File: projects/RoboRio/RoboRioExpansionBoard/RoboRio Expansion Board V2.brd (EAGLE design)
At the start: 56.6 x 77.5 mm, 133 parts, among them J1 RRINTERFACE-FEMALE, J10 SPI_MISO, J11 SPI_MOSI, J12 I2C_SCL, J13 I2C_SDA, J14 UART_TX, J15 UART_RX, J16 LCD, J17 ADC1, J18 ADC2, J19 ADC3, J2 MICROSD-HINGED, J20 ADC4, J21 ADC5, J22 ADC6, J23 ADC7, J25 PWM0, J26 PWM1, J27 PWM2, J28 PWM3, J29 PWM4, J3 51387-0578, J30 PWM5, J31 PWM6, J32 PWM7, J33 PWM8, J34 PWM9, J35 AI0, J36 AI1, J37 AI2, J38 AI3, J39 AO0, J4 GPIO0, J40 AO1, J5 GPIO1, J6 GPIO2, J7 GPIO3, J8 SPI_CS, J9 SPI_CLK, Q1 NPN-SOT416, Q2 NPN-SOT416, Q3 NPN-SOT416, SW1 450-1781-ND, U1 FTS31XS-U, U2 24LC256ST, U3 REG1117, U4 TPS2115APWR, U5 P8X32A-Q44_P, U6 TC54VN43, U7 ADC124S01, U8 ADC124S01, Y1 5MHz

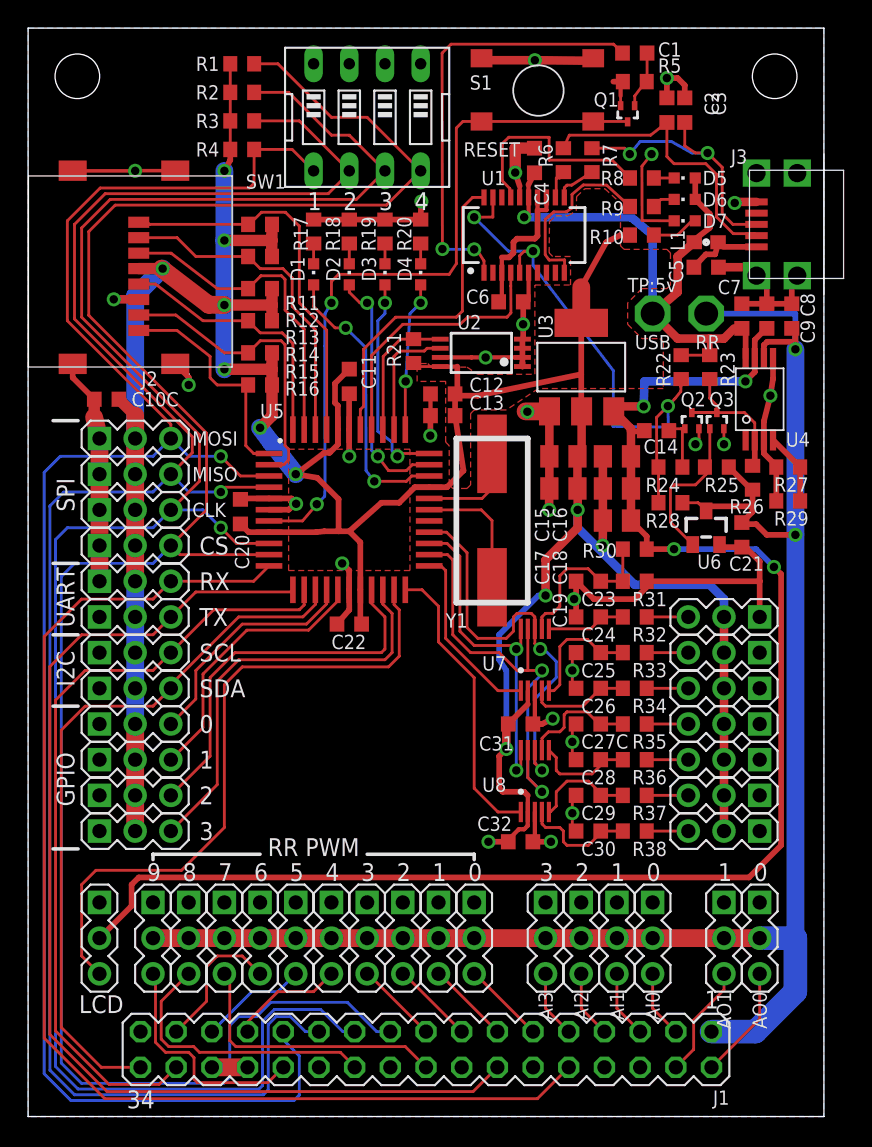
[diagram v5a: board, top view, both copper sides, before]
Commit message: Fixed all DRC errors
Lots of copper movement to deal with clearances, 45° angles, etc.
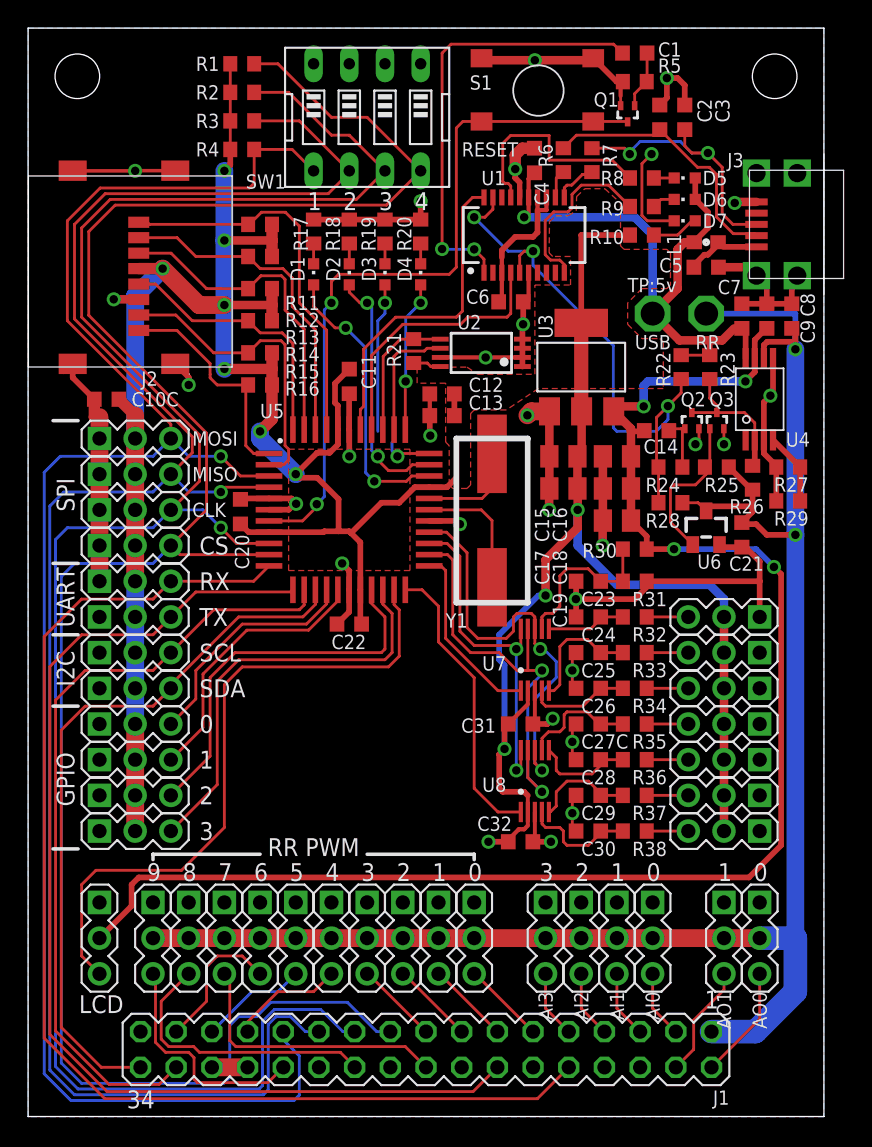
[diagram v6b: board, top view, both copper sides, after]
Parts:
- moved C2 0.72 mm to (45.0, 71.1)
- moved C3 0.51 mm to (46.7, 71.1)
- moved C12 0.05 mm to (29.5, 51.4)
- moved C13 0.05 mm to (29.5, 49.9)
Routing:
- net +3V3: track 244.7 -> 231.8 mm
- net DGND: track 183.5 -> 187.0 mm, vias 26 -> 28
- net N$2: track 21.2 -> 19.2 mm
- net N$20: track 12.2 -> 10.5 mm
- net IO26: track 15.4 -> 14.2 mm
- net PWREN_L: track 40.4 -> 39.8 mm
- net N$27: track 3.62 -> 3.12 mm

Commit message: Fixed stopmask issues with silk
All that is left is labeling the RR AI/AO in the bottom right, and
figuring out how to reorient the text for the other connections.
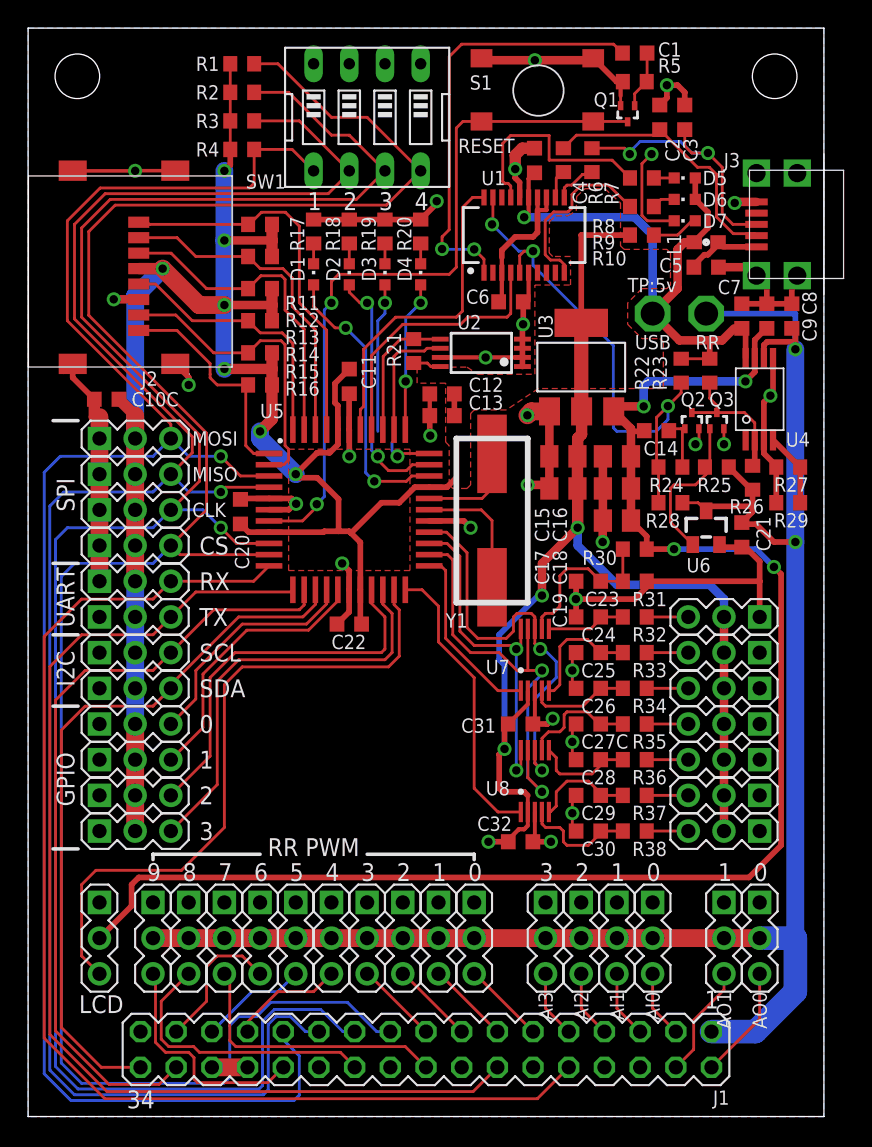
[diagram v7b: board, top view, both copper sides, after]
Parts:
- moved R22 0.25 mm to (46.5, 53.1)
- moved R23 0.25 mm to (48.5, 53.1)
- moved R29 0.13 mm to (54.1, 43.7)
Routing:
- net PWREN_L: track 39.8 -> 37.6 mm
- net +3V3: track 231.8 -> 230.4 mm

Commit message: Small aesthetic changes
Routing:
- net +3V3: track 230.4 -> 249.9 mm
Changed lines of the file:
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@@
 <text x="55.372" y="30.607" size="1.27" layer="51" font="vector" ratio="12" rot="R90" align="bottom-center">3</text>
 <text x="55.372" y="28.067" size="1.27" layer="51" font="vector" ratio="12" rot="R90" align="bottom-center">4</text>
-<text x="3.302" y="36.957" size="1.27" layer="25" font="vector" ratio="12" rot="R270" align="top-center">UART</text>
-<text x="3.302" y="43.053" size="1.27" layer="25" font="vector" ratio="12" rot="R90">SPI</text>
-<text x="3.302" y="31.877" size="1.27" layer="25" font="vector" ratio="12" rot="R90" align="bottom-center">I2C</text>
+<text x="3.302" y="36.703" size="1.27" layer="25" font="vector" ratio="12" rot="SR270" align="top-center">UART</text>
+<text x="3.302" y="42.799" size="1.27" layer="25" font="vector" ratio="12" rot="SR270" align="top-right">SPI</text>
+<text x="3.302" y="31.623" size="1.27" layer="25" font="vector" ratio="12" rot="SR270" align="top-center">I2C</text>
 <wire x1="3.556" y1="34.29" x2="1.778" y2="34.29" width="0.254" layer="25"/>
 <wire x1="3.556" y1="39.37" x2="1.778" y2="39.37" width="0.254" layer="25"/>
@@
 <text x="12.192" y="20.32" size="1.27" layer="25" font="vector" ratio="12" align="center-left">3</text>
 <wire x1="3.556" y1="19.05" x2="1.778" y2="19.05" width="0.254" layer="25"/>
-<text x="3.302" y="24.003" size="1.27" layer="25" font="vector" ratio="12" rot="R90" align="bottom-center">GPIO</text>
+<text x="3.302" y="24.003" size="1.27" layer="25" font="vector" ratio="12" rot="SR270" align="top-center">GPIO</text>
 <text x="12.192" y="40.64" size="1.27" layer="25" font="vector" ratio="12" align="center-left">CS</text>
 <text x="42.672" y="58.674" size="1.016" layer="21" font="vector" ratio="14">TP:5v</text>
@@
 </element>
 <element name="C6" library="resistor" package="C0603K" value=".1uF" x="34.3662" y="57.9882" smashed="yes" rot="R180">
-<attribute name="NAME" x="32.8422" y="58.8622" size="1.016" layer="25" font="vector" ratio="14" rot="R180"/>
+<attribute name="NAME" x="32.8422" y="58.7352" size="1.016" layer="25" font="vector" ratio="14" rot="R180"/>
 <attribute name="VALUE" x="35.1662" y="59.6382" size="1.016" layer="27" rot="R180"/>
 </element>
@@
 </element>
 <element name="R21" library="resistor" package="R0603" value="10k" x="27.432" y="54.483" smashed="yes" rot="R270">
-<attribute name="NAME" x="26.543" y="53.34" size="1.016" layer="25" font="vector" ratio="14" rot="R90"/>
+<attribute name="NAME" x="26.416" y="53.467" size="1.016" layer="25" font="vector" ratio="14" rot="R90"/>
 <attribute name="VALUE" x="25.527" y="55.118" size="1.27" layer="27" rot="R270"/>
 </element>
@@
 <wire x1="33.909" y1="26.162" x2="33.909" y2="27.672" width="0.4064" layer="1"/>
 <wire x1="33.909" y1="27.672" x2="34.177" y2="27.94" width="0.4064" layer="1"/>
+<wire x1="49.53" y1="20.32" x2="49.53" y2="19.304" width="0.6096" layer="16"/>
+<wire x1="49.53" y1="19.304" x2="48.26" y2="18.034" width="0.6096" layer="16"/>
+<wire x1="48.26" y1="18.034" x2="33.274" y2="18.034" width="0.6096" layer="16"/>
+<wire x1="33.274" y1="18.034" x2="32.766" y2="18.542" width="0.6096" layer="16"/>
+<wire x1="32.766" y1="18.542" x2="32.766" y2="19.558" width="0.6096" layer="16"/>
 <wire x1="35.568" y1="21.676" x2="35.56" y2="21.668" width="0" layer="19" extent="1-1"/>
 </signal>
